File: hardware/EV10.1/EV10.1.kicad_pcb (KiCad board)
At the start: 4 copper layers, 72.7 x 89.4 mm, 110 parts, among them J1 Conn_01x02_Socket, J10 Conn_01x08_Socket, J11 Conn_01x06_Female, J13 Conn_01x04_Female, J2 Conn_01x02_Female, J5 Conn_01x02_Socket, J7 Conn_01x04_Female, J8 Conn_01x06_Female, J9 USB_C_Receptacle, SW4 SW_Push, SW5 SW_Push, U1 STM32F405RGTx, U11 ESP32-S3-WROOM-1-N8R2, U13 BM14B(0.8)-24DS-0.4V(53), U2 BQ21040DBVR, U3 CH340C, U4 USBLC6-2P6, U5 STM32F030C8Tx, U6 WM8960CGEFL/RV, U7 TPS63060, Y1 Crystal_GND24

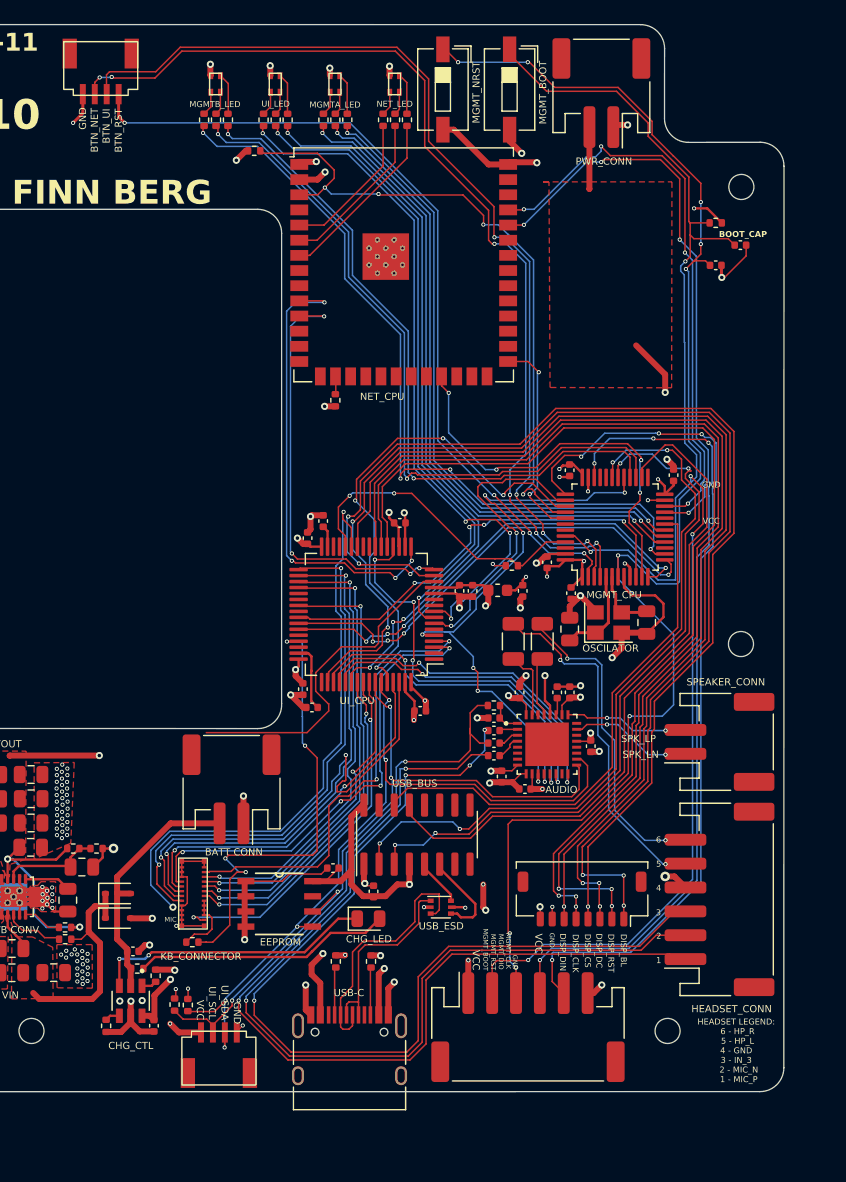
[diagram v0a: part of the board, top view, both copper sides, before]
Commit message: Fix most warnings and errors in EV10.1
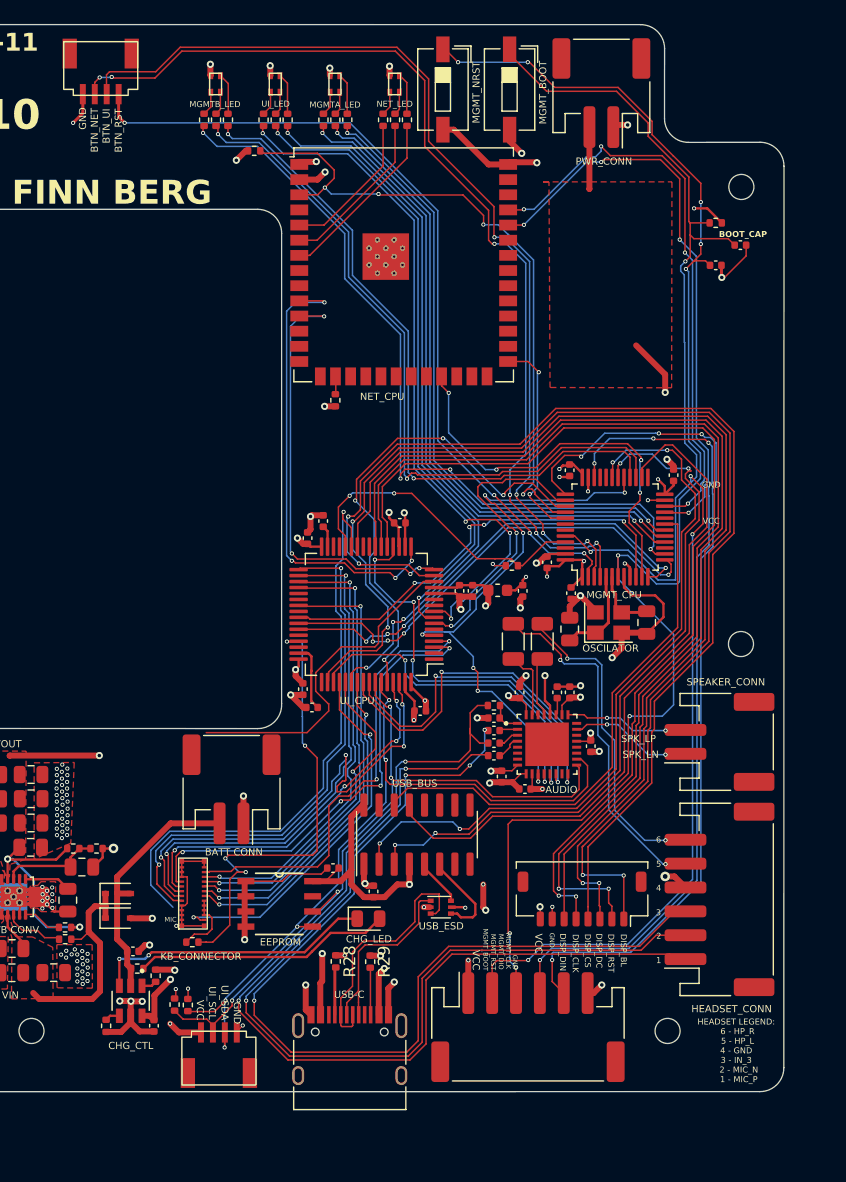
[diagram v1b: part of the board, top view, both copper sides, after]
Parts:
- removed J9: USB_C_Receptacle, Connector_USB:USB_C_Receptacle_HRO_TYPE-C-31-M-12
- removed R2, R3: 5k1, Resistor_SMD:R_0402_1005Metric
- added R28: 5k1, Resistor_SMD:R_0402_1005Metric, F.Cu at (149.1, 134.5)
- added R29: 5k1, Resistor_SMD:R_0402_1005Metric, F.Cu at (152.0, 134.5)
- added USB_C1: TYPE-C-31-M-12, Connector_USB:USB_C_Receptacle_HRO_TYPE-C-31-M-12, F.Cu at (150.3, 143.0)
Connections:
- U1 pad 52: /I2S_ADCDAT -> /KB_ROW7
- U1 pad 53: /I2S_DACDAT -> /KB_COL5
- U1 pad 56: /KB_ROW7 -> /I2S_ADCDAT
- U1 pad 57: /KB_COL5 -> /I2S_DACDAT
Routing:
- net Net-(J9-CC1): track 4.17 -> 0.00 mm
- net Net-(USB_C1-CC1): track 0.00 -> 4.00 mm
- net Net-(J9-CC2): track 3.99 -> 0.00 mm
- net Net-(USB_C1-CC2): track 0.00 -> 3.92 mm
- net /I2S_ADCDAT: track 28.3 -> 30.6 mm
- net /I2S_DACDAT: track 26.7 -> 28.8 mm
- net GND: track 569.0 -> 571.0 mm
- net /KB_COL5: track 26.7 -> 28.2 mm
- net /KB_ROW7: track 30.5 -> 31.6 mm
- net /KB_COL1: track 40.0 -> 40.9 mm, vias 2 -> 4
- net /UI_BOOT: track 42.4 -> 41.6 mm
- net /KB_ROW6: track 28.2 -> 28.9 mm
- net VBUS: track 55.9 -> 55.3 mm
- net /KB_COL2: track 31.0 -> 31.5 mm, vias 2 -> 4
- net /DISP_RSTR: track 86.6 -> 86.5 mm, vias 3 -> 2
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
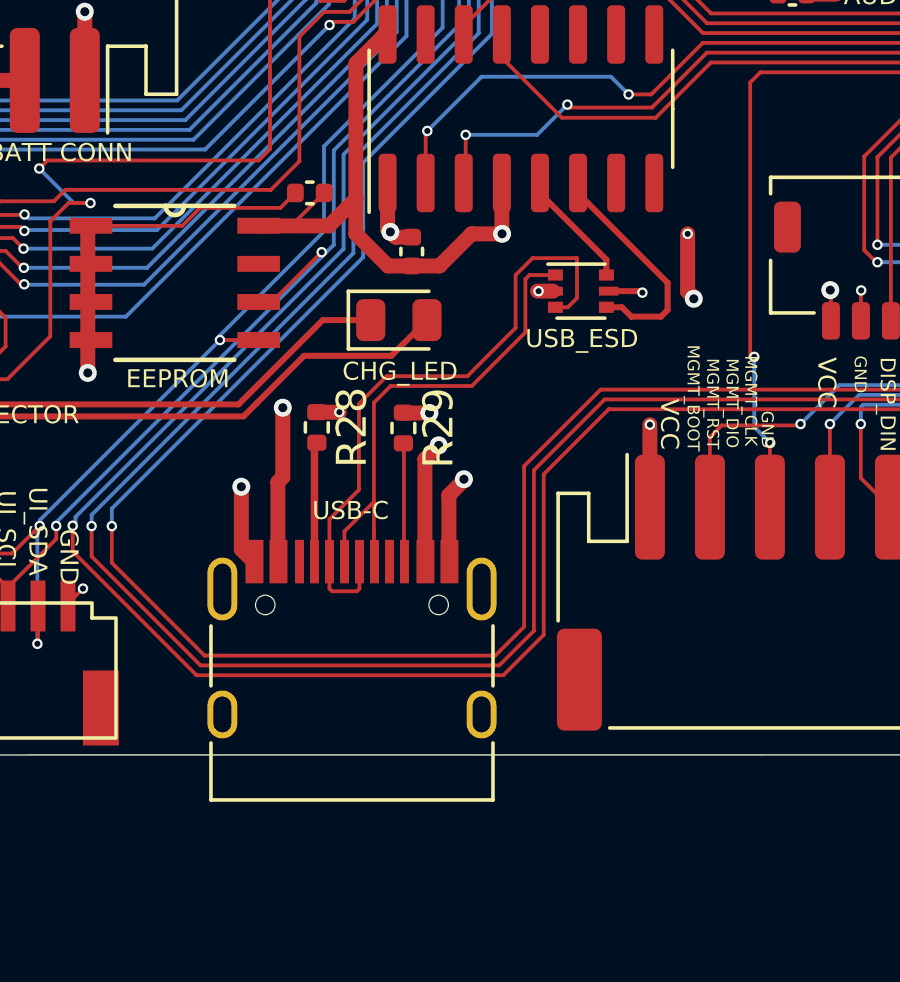
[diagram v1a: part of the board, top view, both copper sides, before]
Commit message: Updated symbols and footprints to be jlcpcb specific
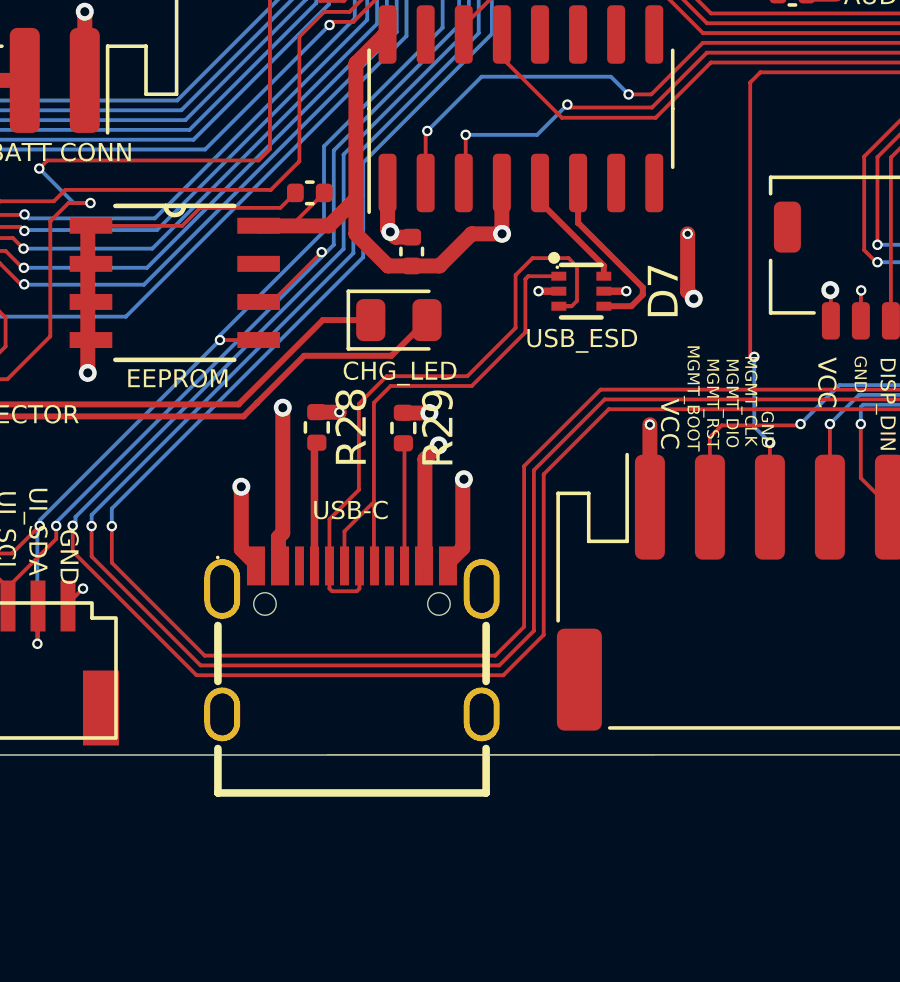
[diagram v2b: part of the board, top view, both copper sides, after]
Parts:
- removed U4: USBLC6-2P6, Package_TO_SOT_SMD:SOT-666
- removed USB_C1: TYPE-C-31-M-12, Connector_USB:USB_C_Receptacle_HRO_TYPE-C-31-M-12
- added D7: USBLC6-2P6_C2827693, jlc_pcb:SOT-666-6_L1.6-W1.2-P0.50-LS1.6-BL, F.Cu at (158.0, 130.0)
- added USB-C1: TYPE-C-31-M-12, footprint:USB-C_SMD-TYPE-C-31-M-12, F.Cu at (150.3, 141.6)
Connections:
- U6 pad 24: unconnected-(U6-SPKGND1-Pad24) -> GND
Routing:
- net /UD-: track 7.73 -> 6.08 mm
- net VBUS: track 55.3 -> 54.7 mm

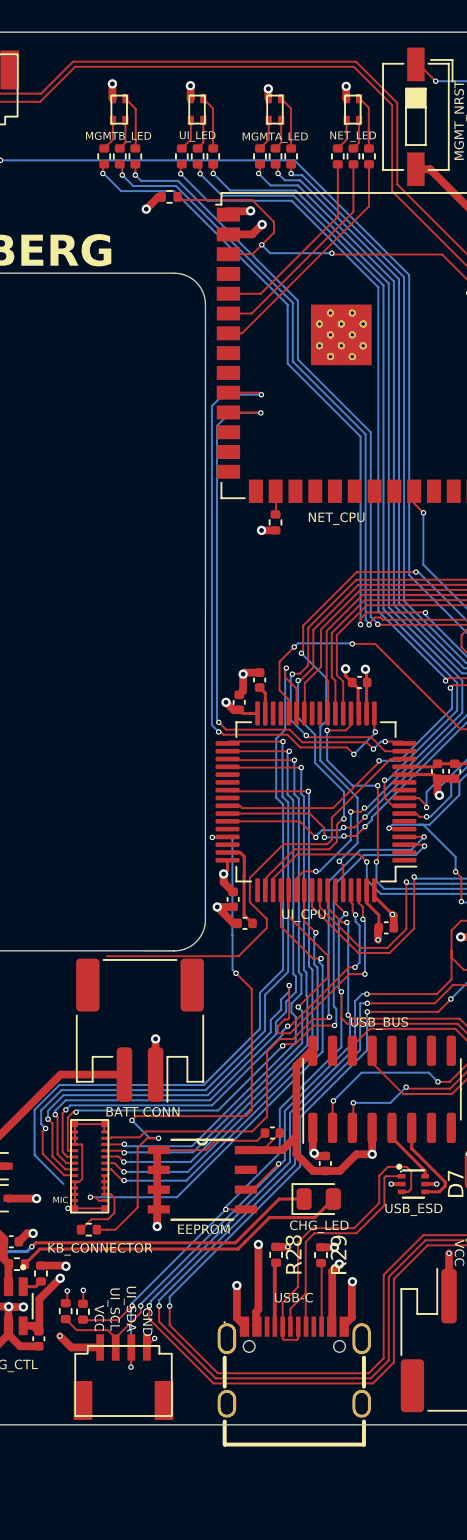
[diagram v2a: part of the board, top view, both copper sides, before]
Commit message: Update jlcpcb labels, and some rotations and positions
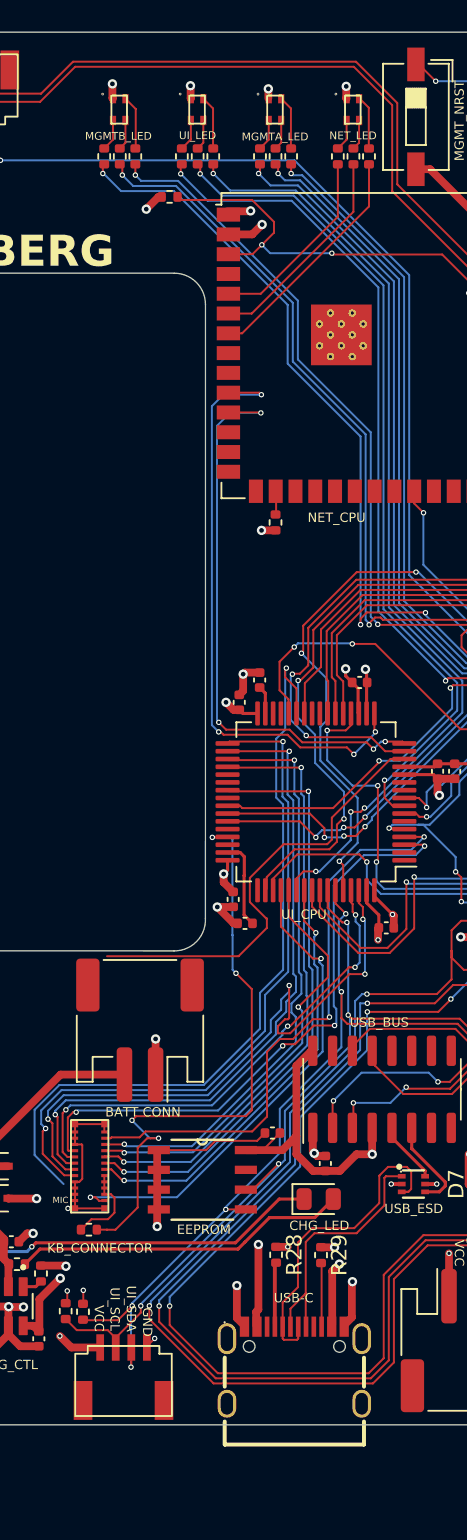
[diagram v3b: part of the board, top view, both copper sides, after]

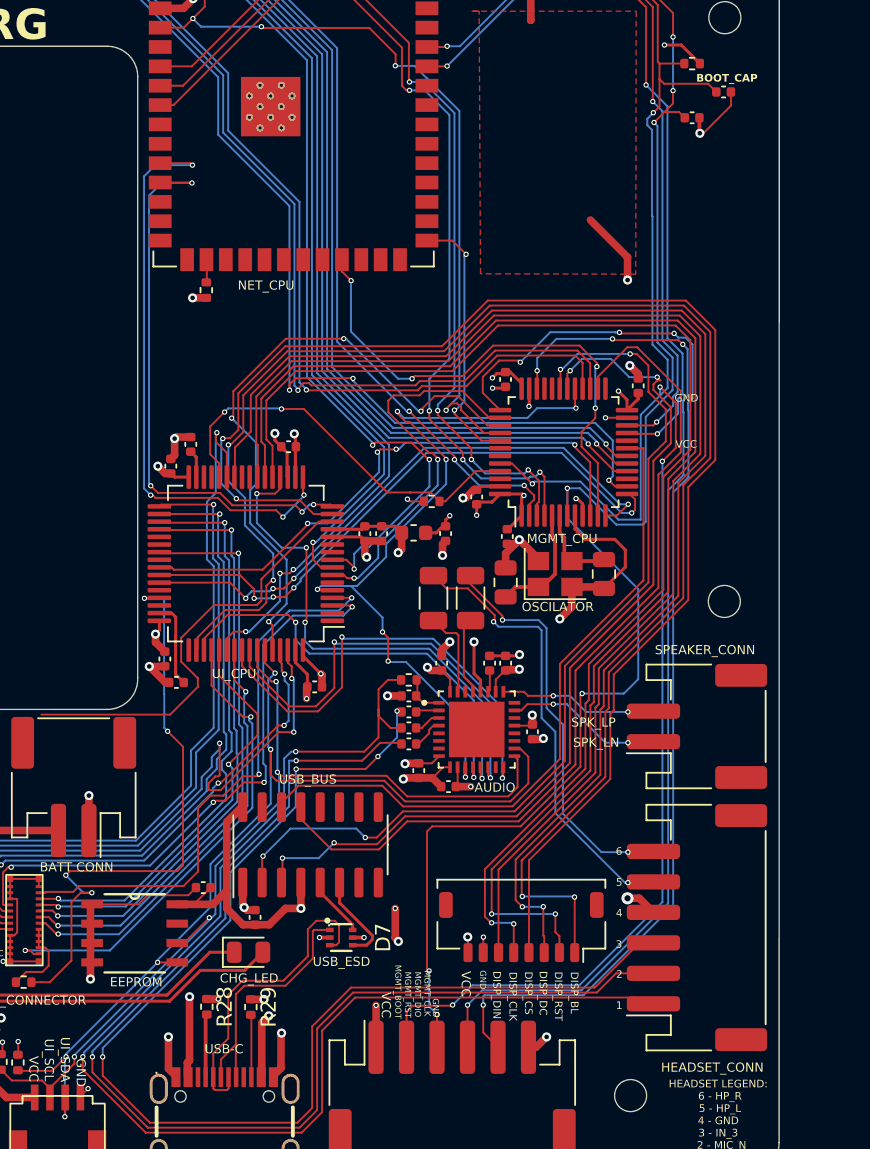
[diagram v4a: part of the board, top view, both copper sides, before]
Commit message: Adding test points
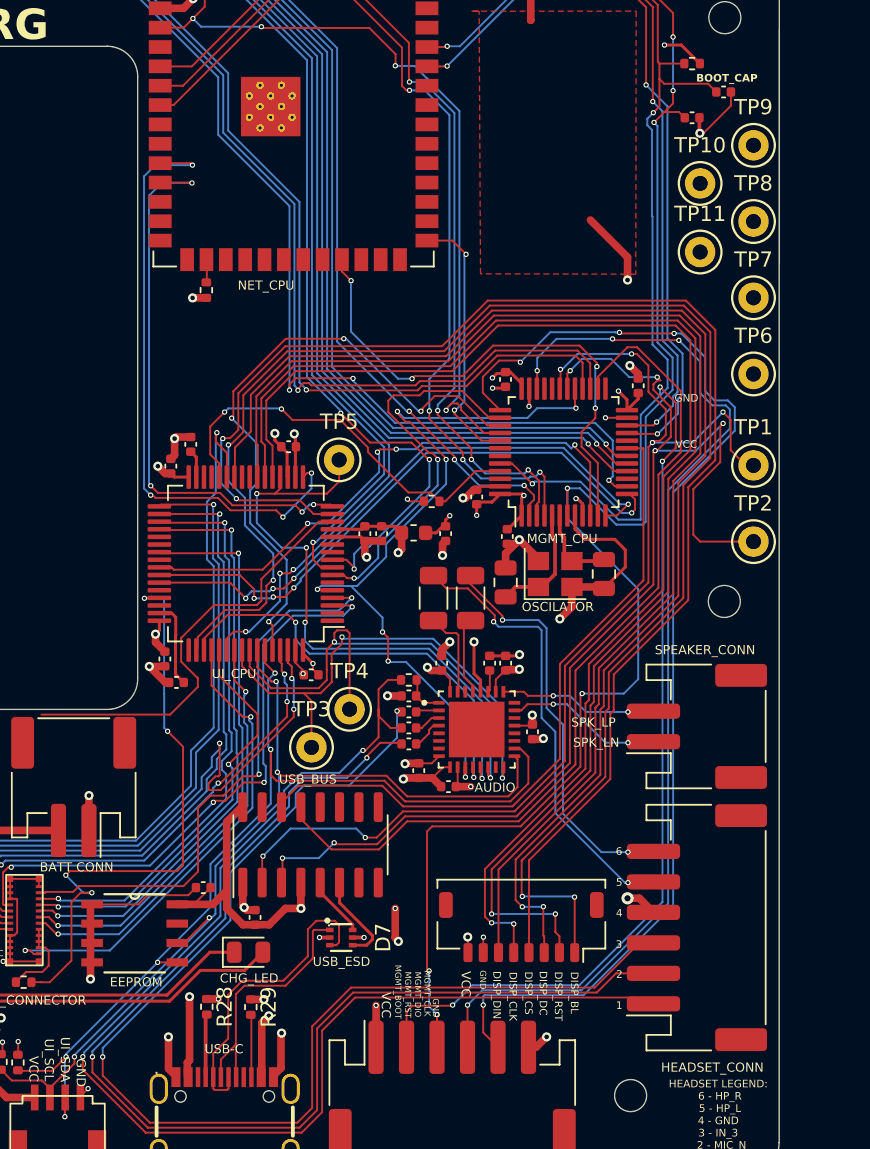
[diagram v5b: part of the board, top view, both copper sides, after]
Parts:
- added TP1: TestPoint_Probe, TestPoint:TestPoint_Keystone_5000-5004_Miniature, F.Cu at (185.0, 99.0)
- added TP10: TestPoint_Probe, TestPoint:TestPoint_Keystone_5000-5004_Miniature, F.Cu at (181.5, 80.5)
- added TP11: TestPoint_Probe, TestPoint:TestPoint_Keystone_5000-5004_Miniature, F.Cu at (181.5, 85.0)
- added TP2: TestPoint_Probe, TestPoint:TestPoint_Keystone_5000-5004_Miniature, F.Cu at (185.0, 104.0)
- added TP3: TestPoint_Probe, TestPoint:TestPoint_Keystone_5000-5004_Miniature, F.Cu at (156.0, 117.5)
- added TP4: TestPoint_Probe, TestPoint:TestPoint_Keystone_5000-5004_Miniature, F.Cu at (158.5, 115.0)
- added TP5: TestPoint_Probe, TestPoint:TestPoint_Keystone_5000-5004_Miniature, F.Cu at (157.8, 98.6)
- added TP6: TestPoint_Probe, TestPoint:TestPoint_Keystone_5000-5004_Miniature, F.Cu at (185.0, 93.0)
- added TP7: TestPoint_Probe, TestPoint:TestPoint_Keystone_5000-5004_Miniature, F.Cu at (185.0, 88.0)
- added TP8: TestPoint_Probe, TestPoint:TestPoint_Keystone_5000-5004_Miniature, F.Cu at (185.0, 83.0)
- added TP9: TestPoint_Probe, TestPoint:TestPoint_Keystone_5000-5004_Miniature, F.Cu at (185.0, 78.0)
- moved C12 0.82 mm to (156.0, 112.7)
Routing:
- net /USB_RX1_MGMT: track 59.9 -> 76.9 mm, vias 4 -> 6
- net /USB_TX1_MGMT: track 61.6 -> 71.4 mm, vias 4 -> 6
- net /I2S_DACLRC: track 33.5 -> 39.5 mm
- net /I2S_DACDAT: track 28.8 -> 34.0 mm
- net /MGMT_SWDIO: track 68.3 -> 71.1 mm
- net /MGMT_SWCLK: track 74.1 -> 76.9 mm
- net /I2S_ADCDAT: track 30.6 -> 32.8 mm
- net /MIC_P: track 85.9 -> 84.7 mm
- net /MIC_N: track 79.0 -> 77.8 mm
- net /UI_RX2_NET: track 39.2 -> 40.4 mm
- net GND: track 571.2 -> 570.2 mm
- net /IN_3: track 80.3 -> 79.4 mm, vias 4 -> 2
- net /KB_COL1: track 40.9 -> 40.3 mm
- net +3.3V: track 458.0 -> 457.5 mm

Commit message: EV10.1 is ready for review
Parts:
- added TP12: P_GND, TestPoint:TestPoint_Keystone_5000-5004_Miniature, F.Cu at (185.0, 73.5)
- TP1: value TestPoint_Probe -> P_USB_TX_MGMT
- TP10, TP11: value TestPoint_Probe -> P_UI_RX_NET
- TP2: value TestPoint_Probe -> P_USB_RX_MGMT
- TP3: value TestPoint_Probe -> P_I2S_ADCDAT
- TP4: value TestPoint_Probe -> P_I2S_DACDAT
- TP5: value TestPoint_Probe -> P_I2S_DACLRC
- TP6: value TestPoint_Probe -> P_UI_TX_MGMT
- TP7: value TestPoint_Probe -> P_UI_RX_MGMT
- TP8: value TestPoint_Probe -> P_NET_TX_MGMT
- TP9: value TestPoint_Probe -> P_NET_RX_MGMT
- moved TP9 8.73 mm to (181.5, 86.0)
- moved TP11 7.83 mm to (185.0, 78.0)
- moved TP7 5.02 mm to (184.5, 93.0)
- moved TP6 3.54 mm to (184.5, 89.5)
- moved C36 1.54 mm to (181.5, 74.5)
- moved TP1 1.50 mm to (185.0, 100.5)
- moved C35 0.53 mm to (181.5, 76.2)
- moved R10 0.53 mm to (181.5, 72.6)
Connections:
- U13 pad 2: GND -> +3.3V
- U13 pad 3: GND -> /KB_MIC
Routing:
- net /UI_RX1_MGMT: track 38.7 -> 96.5 mm, vias 4 -> 5
- net /UI_TX1_MGMT: track 39.3 -> 95.2 mm, vias 4 -> 6
- net /UI_RX2_NET: track 40.4 -> 92.3 mm, vias 4 -> 5
- net /UI_TX2_NET: track 37.1 -> 87.7 mm, vias 4 -> 5
- net /USB_TX1_MGMT: track 71.4 -> 82.0 mm
- net /NET_TX1_MGMT: track 48.9 -> 55.6 mm, vias 4 -> 5
- net /NET_RX1_MGMT: track 49.0 -> 54.3 mm
- net /NET_BOOT: track 17.8 -> 22.5 mm
- net +3.3V: track 457.5 -> 461.6 mm, vias 28 -> 29
- net GND: track 570.2 -> 573.6 mm, vias 155 -> 154
- net /MGMT_NRST: track 121.2 -> 122.4 mm
- net /MGMT_BOOT: track 129.6 -> 128.6 mm
- net /KB_ROW1: track 45.1 -> 44.2 mm
- net /KB_ROW2: track 43.4 -> 42.8 mm
- net /USB_RX1_MGMT: track 76.9 -> 77.4 mm
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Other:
- board text added: "2024-03"
- board text added: "EV10.1"
- board text added: "FINN BERG BRETT REGNIER"
- board text removed: "2023-11"
- board text removed: "EV10"
- board text removed: "FINN BERG"
